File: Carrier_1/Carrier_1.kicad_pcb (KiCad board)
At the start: 2 copper layers, 17 x 13.5 mm, 7 parts, among them J1 CH1, J2 CH2, J3 HV, J4 GND, U1 LGAD_2_pad

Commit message: Several updates
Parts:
- removed REF** (x2): MountingHole_2.1mm, MountingHole:MountingHole_2.1mm
- added H1: MountingHole, MountingHole:MountingHole_2.1mm, F.Cu at (-6.00, -10.0)
- added H2: MountingHole, MountingHole:MountingHole_2.1mm, F.Cu at (6.00, -10.0)
- renumbered J3 to J2, J2 to J3
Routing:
- net GND: track 14.6 -> 4.11 mm
- net /HV: track 11.3 -> 9.45 mm, vias 31 -> 1
- added copper zone on B.Cu, net GND
- removed copper zone on B.Cu, net /HV
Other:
- board size 17 x 13.5 mm -> 17 x 16.5 mm

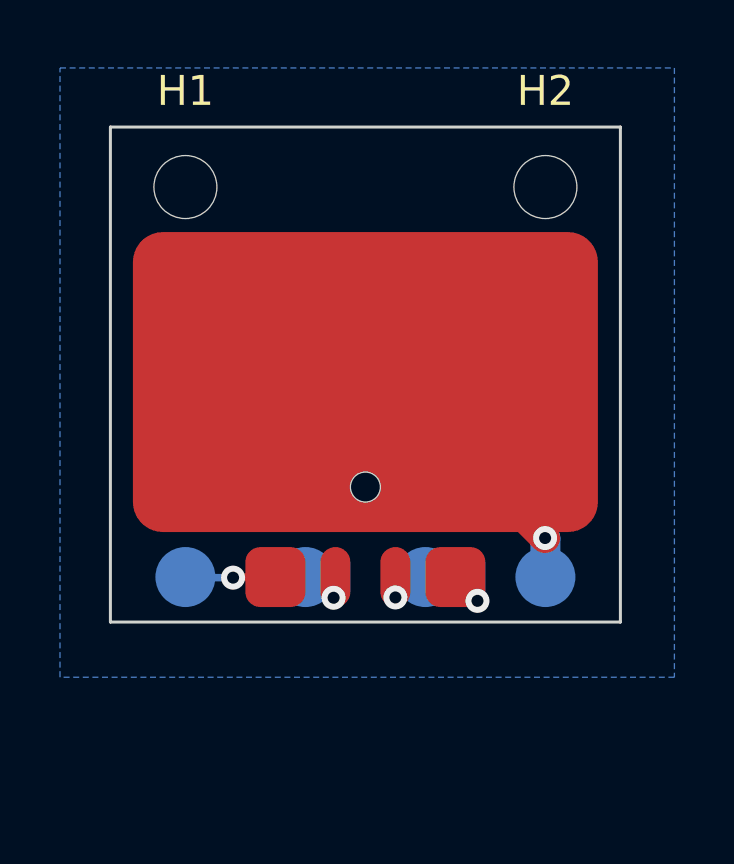
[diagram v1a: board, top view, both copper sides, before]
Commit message: Added mounting holes for testing different type of connection
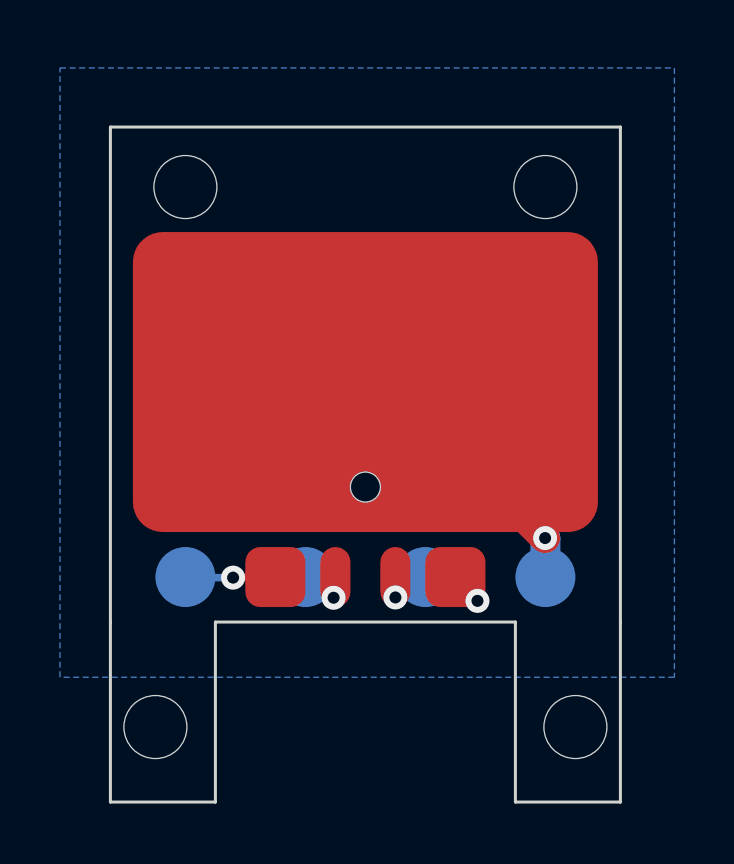
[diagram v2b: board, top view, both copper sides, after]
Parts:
- added H3: MountingHole, MountingHole:MountingHole_2.1mm, F.Cu at (7.00, 8.00)
- added H4: MountingHole, MountingHole:MountingHole_2.1mm, F.Cu at (-7.00, 8.00)
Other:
- board size 17 x 16.5 mm -> 17 x 22.5 mm
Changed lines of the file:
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@@
   (footprint "chubut:LGAD" (layer "F.Cu")
     (at 0 0)
-    (property "Sheetfile" "Carrier_1.kicad_sch")
+    (property "Sheetfile" "File: Carrier_1.kicad_sch")
     (property "Sheetname" "")
     (attr smd)
@@
     (descr "Mounting Hole 2.1mm, no annular")
     (tags "mounting hole 2.1mm no annular")
-    (property "Sheetfile" "Carrier_1.kicad_sch")
+    (property "Sheetfile" "File: Carrier_1.kicad_sch")
     (property "Sheetname" "")
     (attr exclude_from_pos_files)
-    (fp_text reference "H1" (at 0 -3.2) (layer "F.SilkS")
+    (fp_text reference "H1" (at 0 -3.2) (layer "F.SilkS") hide
+      (effects (font (size 1 1) (thickness 0.15)))
+    )
+    (fp_text value "MountingHole" (at 0 3.2) (layer "F.Fab")
+      (effects (font (size 1 1) (thickness 0.15)))
+    )
+    (fp_text user "${REFERENCE}" (at 0 0) (layer "F.Fab")
+      (effects (font (size 1 1) (thickness 0.15)))
+    )
+    (fp_circle (center 0 0) (end 2.1 0) (layer "Cmts.User") (width 0.15) (fill none))
+    (fp_circle (center 0 0) (end 2.35 0) (layer "F.CrtYd") (width 0.05) (fill none))
+    (pad "" np_thru_hole circle (at 0 0) (size 2.1 2.1) (drill 2.1) (layers *.Cu *.Mask))
+  )
+  (footprint "MountingHole:MountingHole_2.1mm" (layer "F.Cu")
+    (at 7 8)
+    (descr "Mounting Hole 2.1mm, no annular")
+    (tags "mounting hole 2.1mm no annular")
+    (property "Sheetfile" "File: Carrier_1.kicad_sch")
+    (property "Sheetname" "")
+    (attr exclude_from_pos_files)
+    (fp_text reference "H3" (at 0 -3.2) (layer "F.SilkS") hide
+      (effects (font (size 1 1) (thickness 0.15)))
+    )
+    (fp_text value "MountingHole" (at 0 3.2) (layer "F.Fab")
+      (effects (font (size 1 1) (thickness 0.15)))
+    )
+    (fp_text user "${REFERENCE}" (at 0 0) (layer "F.Fab")
+      (effects (font (size 1 1) (thickness 0.15)))
+    )
+    (fp_circle (center 0 0) (end 2.1 0) (layer "Cmts.User") (width 0.15) (fill none))
+    (fp_circle (center 0 0) (end 2.35 0) (layer "F.CrtYd") (width 0.05) (fill none))
+    (pad "" np_thru_hole circle (at 0 0) (size 2.1 2.1) (drill 2.1) (layers *.Cu *.Mask))
+  )
+  (footprint "MountingHole:MountingHole_2.1mm" (layer "F.Cu")
+    (at -7 8)
+    (descr "Mounting Hole 2.1mm, no annular")
+    (tags "mounting hole 2.1mm no annular")
+    (property "Sheetfile" "File: Carrier_1.kicad_sch")
+    (property "Sheetname" "")
+    (attr exclude_from_pos_files)
+    (fp_text reference "H4" (at 0 -3.2) (layer "F.SilkS") hide
       (effects (font (size 1 1) (thickness 0.15)))
     )
@@
     (descr "Mounting Hole 2.1mm, no annular")
     (tags "mounting hole 2.1mm no annular")
-    (property "Sheetfile" "Carrier_1.kicad_sch")
+    (property "Sheetfile" "File: Carrier_1.kicad_sch")
     (property "Sheetname" "")
     (attr exclude_from_pos_files)
-    (fp_text reference "H2" (at 0 -3.2) (layer "F.SilkS")
+    (fp_text reference "H2" (at 0 -3.2) (layer "F.SilkS") hide
       (effects (font (size 1 1) (thickness 0.15)))
     )
@@
   (footprint "chubut:MILL-MAX_0965-0-15-20-80-14-11-0_contact" (layer "B.Cu")
     (at -2 3 180)
-    (property "Sheetfile" "Carrier_1.kicad_sch")
+    (property "Sheetfile" "File: Carrier_1.kicad_sch")
     (property "Sheetname" "")
     (attr smd)
@@
   (footprint "chubut:MILL-MAX_0965-0-15-20-80-14-11-0_contact" (layer "B.Cu")
     (at 2 3 180)
-    (property "Sheetfile" "Carrier_1.kicad_sch")
+    (property "Sheetfile" "File: Carrier_1.kicad_sch")
     (property "Sheetname" "")
     (attr smd)
@@
   (footprint "chubut:MILL-MAX_0965-0-15-20-80-14-11-0_contact" (layer "B.Cu")
     (at -6 3 180)
-    (property "Sheetfile" "Carrier_1.kicad_sch")
+    (property "Sheetfile" "File: Carrier_1.kicad_sch")
     (property "Sheetname" "")
     (zone_connect 2)
@@
   (footprint "chubut:MILL-MAX_0965-0-15-20-80-14-11-0_contact" (layer "B.Cu")
     (at 6 3 180)
-    (property "Sheetfile" "Carrier_1.kicad_sch")
+    (property "Sheetfile" "File: Carrier_1.kicad_sch")
     (property "Sheetname" "")
     (attr smd)
@@
       (net 4 "/HV") (pinfunction "Pin_1") (pintype "passive"))
   )
-  (gr_rect (start -8.5 -12) (end 8.5 4.5) (layer "Edge.Cuts") (width 0.1) (fill none))
+  (gr_line (start 8.5 4.5) (end 8.5 10.5) (layer "Edge.Cuts") (width 0.1))
+  (gr_line (start 8.5 10.5) (end 5 10.5) (layer "Edge.Cuts") (width 0.1))
+  (gr_line (start -5 4.5) (end 5 4.5) (layer "Edge.Cuts") (width 0.1))
+  (gr_line (start -8.5 -12) (end 8.5 -12) (layer "Edge.Cuts") (width 0.1))
+  (gr_line (start -5 10.5) (end -5 4.5) (layer "Edge.Cuts") (width 0.1))
+  (gr_line (start -8.5 4.5) (end -8.5 10.5) (layer "Edge.Cuts") (width 0.1))
+  (gr_line (start 8.5 -12) (end 8.5 4.5) (layer "Edge.Cuts") (width 0.1))
+  (gr_line (start -8.5 10.5) (end -5 10.5) (layer "Edge.Cuts") (width 0.1))
+  (gr_line (start 5 10.5) (end 5 4.5) (layer "Edge.Cuts") (width 0.1))
+  (gr_line (start -8.5 4.5) (end -8.5 -12) (layer "Edge.Cuts") (width 0.1))
   (segment (start 3 3.05808) (end 3.735539 3.793619) (width 0.25) (layer "F.Cu") (net 1))
   (segment (start -4.39 3) (end -4.41 3.02) (width 0.25) (layer "F.Cu") (net 1))
